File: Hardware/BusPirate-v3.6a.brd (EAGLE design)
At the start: 53.3 x 30.5 mm, 50 parts, among them IC1 PIC24FJ64GA002-I/SSSS-ALTERNA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, IC2 FT232RLSSOP, IC3 4066D, J1 USBSMD

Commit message: First commit of v3.6a
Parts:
- removed C12: 0.1uF, SparkFun:0402-CAP
- removed I/O: M05X2SHD_SMD, SparkFun:2X5-SHROUDED_SMD
- removed J1: USBSMD, SparkFun:USB-MINIB
- removed JP2: LOGO-SFENEW, SparkFun:SFE-NEW-WEBLOGO
- removed JP3, JP4: FIDUCIAL1X2, SparkFun:FIDUCIAL-1X2
- removed LED6: BLUE, SparkFun:LED-0603
- removed LED9: YELLOW, SparkFun:LED-0603
- removed R10, R17: 1k1, SparkFun:0402-RES
- removed R11: 390R, SparkFun:0402-RES
- removed R12, R13, R14, R15, R18, R20, R7, R9: 10k, SparkFun:0402-RES
- removed R16, R8: 2k, SparkFun:0402-RES
- removed VR4: 5V, SparkFun:SOT23-5
- added C3: 0.1uF, SparkFun-Capacitors:0603-CAP
- added FID1, FID2: FIDUCIAL1X2, SparkFun-Aesthetics:FIDUCIAL-1X2
- added FRAME1: FRAME-LETTER, SparkFun-Aesthetics:CREATIVE_COMMONS
- added L1: 700mA+ ferrite, wuerth-elektronik:WE-KI_0805_B
- added LED1A, LED2A, LED3, LED3A, LED4A: (no value), led:CHIP-LED0805
- added LOGO1: SFE_LOGO_NAME_FLAME.1_INCH, SparkFun-Aesthetics:SFE_LOGO_NAME_FLAME_.1
- added LOGO2: OSHW-LOGOL, SparkFun-Aesthetics:OSHW-LOGO-L
- added RN1, RN2, RN3: 10k, Testing:4XARRAY
- added U$3: (no value), dp_devices:DP_LOGO_ART_1X1
- added VR1: MIC5205 3V3, SparkFun-PowerIC:SOT23-5
- C1, C6: value 2.2uF -> 0.1uF; device SparkFun:0402-CAP -> SparkFun-Capacitors:0603-CAP
- C10: value 0.1uF -> 10uF; device SparkFun:0402-CAP -> rcl:SMC_A
- C11: device SparkFun:EIA3216 -> rcl:SMC_A
- C2, C4: device SparkFun:0402-CAP -> SparkFun-Capacitors:0603-CAP
- C5: device SparkFun:0402-CAP -> dp_devices:C603
- C7: value 10uF -> 0.1uF; device SparkFun:EIA3216 -> SparkFun-Capacitors:0603-CAP
- C8: value 2.2uF -> 1uF; device SparkFun:0402-CAP -> dp_devices:C603
- C9: value 0.1uF -> 1uF; device SparkFun:0402-CAP -> dp_devices:C603
- IC1: value PIC24FJ64GA002-I/SSSS-ALTERNATE -> PIC24FJ64GA002; device microchip-pic24:SSOP28DB -> dp_devices:SSOP28
- IC2: value FT232RLSSOP -> FT232RL-BASICSSOP; device SparkFun:SSOP28DB -> SparkFun-DigitalIC:SSOP28DB
- IC3: value 4066D -> 4066; device 40xx:SO14 -> 40xx:TSSOP14
- ICSP: value M05X1PTH -> (none); device SparkFun:1X05 -> SparkFun-Connectors:1X05
- JP1: value LOGO-SFENEW -> (none); device SparkFun:SFE-NEW-WEBLOGO -> SparkFun-Connectors:2X5-SHROUDED_SMD
- LED1, LED4: value RED -> (none); device SparkFun:LED-0603 -> led:CHIP-LED0805
- LED2: value GREEN -> (none); device SparkFun:LED-0603 -> led:CHIP-LED0805
- R1, R5: value 10k -> 2.0k; device SparkFun:0402-RES -> SparkFun-Resistors:0603-RES
- R2: value 1k1 -> 1K; device SparkFun:0402-RES -> SparkFun-Resistors:0603-RES
- R3: value 390R -> 1K; device SparkFun:0402-RES -> SparkFun-Resistors:0603-RES
- R4, R6: value 10k -> 1K; device SparkFun:0402-RES -> SparkFun-Resistors:0603-RES
- U$2: value CREATIVE_COMMONS -> USB-MINIB-5PIN; device SparkFun:CREATIVE_COMMONS -> SparkFun-Connectors:USB-MINIB
- VR2: value 3.3V -> MIC5205 3V3; device SparkFun:SOT23-5 -> SparkFun-PowerIC:SOT23-5
- VR3: value 3.3V -> MIC5205 5V0; device SparkFun:SOT23-5 -> SparkFun-PowerIC:SOT23-5
- moved JP1 53.2 mm to (51.5, 18.5)
- moved C8 31.0 mm to (33.5, 27.0), turned to 270 degrees
- moved U$2 30.1 mm to (5.25, 18.5)
- moved U$1 25.6 mm to (13.3, 2.54), flipped to the top
- moved VR2 22.6 mm to (30.0, 27.0), turned to 270 degrees
- moved C10 20.7 mm to (16.5, 27.0), turned to 270 degrees
- moved C9 19.1 mm to (25.4, 27.0)
- moved R6 18.1 mm to (40.0, 34.5), turned to 180 degrees
- moved LED2 17.8 mm to (35.0, 34.5), turned to 270 degrees
- moved R3 16.9 mm to (20.0, 34.5), turned to 180 degrees
- moved R1 16.7 mm to (21.8, 7.66)
- moved R4 15.8 mm to (30.0, 34.5), turned to 180 degrees
- moved C6 14.8 mm to (17.9, 7.66), turned to 180 degrees
- moved C2 13.1 mm to (25.6, 9.46), turned to 180 degrees
- moved ICSP 12.9 mm to (35.1, 3.50), turned to 180 degrees
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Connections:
- removed net MCLR: IC1.1, ICSP.1, R16.1
- removed net N$10: LED2.C, R17.2
- removed net N$11: IC2.22, R2.1
- removed net N$15: IC2.15, J1.D+
- removed net N$16: IC2.16, J1.D-
- removed net N$8: IC2.23, R17.1
- removed net SWV33: C1.1, I/O.9, R3.1, R4.2, VR3.5
- removed net SWV50: C6.1, I/O.8, R15.2, VR4.5
- removed net TP1: IC1.7
- removed net TP2: IC1.6
- removed net V+: C12.1, C5.1, C7.A, IC2.20, IC3.14, J1.VBUS, LED2.A, LED6.A, R1.2, R10.1, VR2.1, VR2.3, VR3.1, VR4.1
- new net !MCLR: IC1.1, ICSP.5, R1.1
- new net $N26: L1.2, U$2.VBUS
- new net 5V: C10.+, C3.1, C4.1, IC2.20, IC3.14, L1.1, RN3.5, VR1.1, VR1.3, VR2.1, VR3.1
- new net D+: IC2.15, U$2.D+
- new net D-: IC2.16, U$2.D-
- new net RXLED: IC2.22, LED4.C, LED4A.C
- new net SW3V3: C8.1, JP1.2, R6.2, RN1.6, VR2.5
- new net SW5V0: C9.1, JP1.3, RN1.8, VR3.5
- net ADC: now also JP1.4, RN2.6; no longer I/O.7, R7.2
- net ADC1: now also RN2.3, RN2.4; no longer R6.1, R7.1
- net ADC2: now also RN2.1, RN2.2; no longer R12.1, R13.1
- net ADC3: now also RN1.3, RN1.4; no longer R4.1, R5.1
- net ADC4: now also RN1.1, RN1.2; no longer R14.1, R15.1
- net AUX1: now also JP1.6; no longer I/O.5
- net CLK: now also JP1.7, RN3.1; no longer I/O.4, R9.2
- net CS: now also JP1.9, RN3.3; no longer I/O.2, R18.2
- net GND: now also C10.-, C11.-, C3.2, C7.2, IC1.6, IC1.7, JP1.1, LED1A.C, LED2.C, LED2A.C, LED3.C, LED3A.C, RN1.5, RN1.7, RN2.5, RN2.7, U$2.GND, VR1.2; no longer C10.2, C11.C, C12.2, C7.C, I/O.10, J1.GND, LED4.C, LED9.C, R13.2, R14.2, R5.2, R6.2, VR4.2
- net LD1: now also R4.2; no longer R11.1
- net MISO: now also JP1.10, RN3.2; no longer I/O.1, R20.2
- net MOSI: now also JP1.8, R5.1; no longer I/O.3, R8.2
- net N$1: now also R5.2; no longer R8.1
- net N$13: now also LED4.A, LED4A.A, R3.1; no longer LED6.C, R2.2
- net N$18: now also LED3.A, LED3A.A, R6.1; no longer LED9.A, R3.2
- net N$2: now also IC3.9, RN3.6; no longer IC3.3, R9.1
- net N$3: now also C11.+; no longer C11.A
- net N$4: now also RN3.7; no longer R20.1
- net N$5: now also IC3.3, RN3.8; no longer IC3.9, R18.1
- net N$6: now also LED2.A, LED2A.A, R4.1; no longer LED4.A, R11.2
- net N$7: now also LED1A.A, R2.1; no longer R10.2
- net N$9: now also C5.1; no longer C9.1
- net PGC: now also ICSP.1; no longer ICSP.5
- net PGD: now also ICSP.2; no longer ICSP.4
- net PULLUPEN: now also RN3.4; no longer R1.1
- net VCC: now also C1.1, C6.1, C7.1, ICSP.4, R1.2, R2.2, R3.2, VR1.5; no longer C10.1, C4.1, C8.1, ICSP.2, R16.2, VR2.5
- net VEXTERN: now also JP1.5, RN2.8; no longer I/O.6, R12.2
- net VREGEN: now also VR2.3; no longer VR4.3
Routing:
- net V+: track 111.2 -> 0.00 mm, vias 5 -> 0
- net 5V: track 0.00 -> 66.5 mm, vias 0 -> 4
- net SW3V3: track 0.00 -> 45.7 mm
- net SWV50: track 42.2 -> 0.00 mm, vias 3 -> 0
- net SW5V0: track 0.00 -> 40.2 mm, vias 0 -> 3
- net RXLED: track 0.00 -> 32.7 mm, vias 0 -> 2
- net SWV33: track 32.2 -> 0.00 mm
- net VCC: track 89.8 -> 115.1 mm, vias 4 -> 3
- net !MCLR: track 0.00 -> 22.1 mm, vias 0 -> 2
- net N$8: track 22.0 -> 0.00 mm, vias 2 -> 0
- net N$11: track 21.5 -> 0.00 mm, vias 2 -> 0
- net MCLR: track 19.8 -> 0.00 mm, vias 2 -> 0
- net D-: track 0.00 -> 9.90 mm
- net N$5: track 7.16 -> 17.1 mm, vias 0 -> 2
- net N$1: track 12.5 -> 22.1 mm, vias 0 -> 2
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- added copper zone on layer 1, net $N26
- added copper zone on layer 1, net 5V
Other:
- board size 53.3 x 30.5 mm -> 60 x 37 mm
- board text added: "!MLCR"
- board text added: "+3V3"
- board text added: "2011"
- board text added: "3V3"
- board text added: "All units in mm"
- board text added: "BPv3.6a"
- board text added: "I+S"
- board text added: "Ian Lesnet http://dangerousprototypes.com"
- board text added: "JUN 2012"
- board text added: "Revised by: Brent Wilkins (Based on BP v3.6a)"
- board text added: "VPU"
- board text added: "v.trocio"
- board text added: "v01"
- board text added: "v3.6a"
- board text removed: "+3.3V"
- board text removed: "+3v"
- board text removed: "+5v"
- board text removed: "2/10/2010"
- board text removed: "AUX1"
- board text removed: "BPv3"
- board text removed: "BPv3a"
- board text removed: "Based on design by"
- board text removed: "CLOCK"
- board text removed: "DATA"
- board text removed: "DangerousPrototypes.com"
- board text removed: "Fulfillment by"
- board text removed: "ICSP"
- board text removed: "Layout for SparkFun Electronics by Chris Taylor"
- board text removed: "RX"
- board text removed: "SEP 2009"
- board text removed: "Seeed Studio"
- board text removed: "TX"
- board text removed: "VCC"
- board text removed: "Vpu"
- board text removed: "dangerousprototypes.com"
- board text removed: "www.seeedstudio.com"

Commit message: Finished inital DFM
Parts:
- removed IC3: 4066, 40xx:TSSOP14
- removed LED1A, LED2A, LED3A, LED4A: (no value), led:CHIP-LED0805
- removed RN1, RN2: 10k, Testing:4XARRAY
- added LED5, LED6, LED7, LED8: RED, SparkFun-LED:LED-0603
- added R10, R11: 2.0k, SparkFun-Resistors:0603-RES
- added R7, R9: 1K, SparkFun-Resistors:0603-RES
- added R8: 0.27, SparkFun-Resistors:0603
- added U3: PIC24FJ64GA002, Testing:SSOP28
- C10, C11: value 10uF -> 0.1uF; device rcl:SMC_A -> SparkFun-Capacitors:0603-CAP
- C3, C4, C7: value 0.1uF -> 10uF; device SparkFun-Capacitors:0603-CAP -> SparkFun-Capacitors:0805-CAP
- C5: device dp_devices:C603 -> SparkFun-Capacitors:0603-CAP
- C8, C9: value 1uF -> 10uF; device dp_devices:C603 -> SparkFun-Capacitors:0805-CAP
- IC1: value PIC24FJ64GA002 -> 4066; device dp_devices:SSOP28 -> 40xx:TSSOP14
- L1: value 700mA+ ferrite -> 1A Ferrite; device wuerth-elektronik:WE-KI_0805_B -> SparkFun-Passives:0603
- LED1, LED2, LED3, LED4: value (none) -> RED; device led:CHIP-LED0805 -> SparkFun-LED:LED-0603
- LOGO1: value SFE_LOGO_NAME_FLAME.1_INCH -> OSHW-LOGOL; device SparkFun-Aesthetics:SFE_LOGO_NAME_FLAME_.1 -> SparkFun-Aesthetics:OSHW-LOGO-L
- LOGO2: value OSHW-LOGOL -> SFE_LOGO_NAME_FLAME.1_INCH; device SparkFun-Aesthetics:OSHW-LOGO-L -> SparkFun-Aesthetics:SFE_LOGO_NAME_FLAME_.1
- R1, R5: value 2.0k -> 0.27; device SparkFun-Resistors:0603-RES -> SparkFun-Resistors:0603
- R2, R3: value 1K -> 10k; device SparkFun-Resistors:0603-RES -> Testing:4XARRAY
- moved C3 48.2 mm to (4.47, 26.9), turned to 270 degrees
- moved R2 32.2 mm to (41.1, 26.1), turned to 270 degrees
- moved C6 30.8 mm to (48.6, 7.55), turned to 0 degrees
- moved LED3 30.0 mm to (15.0, 34.5)
- moved R6 30.0 mm to (10.0, 34.5)
- moved C7 29.1 mm to (32.9, 27.0)
- moved R1 27.0 mm to (2.95, 26.9), turned to 270 degrees
- moved C11 25.3 mm to (11.9, 16.6), turned to 270 degrees
- moved R3 25.1 mm to (41.1, 21.0), turned to 270 degrees
- moved C4 19.8 mm to (16.5, 27.3), turned to 270 degrees
- moved C10 19.4 mm to (17.9, 7.66), turned to 180 degrees
- moved IC1 16.9 mm to (43.7, 5.63)
- moved C9 16.2 mm to (36.7, 15.3), turned to 45 degrees
- moved R5 14.0 mm to (34.5, 27.0), turned to 270 degrees
- moved LOGO1 13.4 mm to (9.78, 18.5), flipped to the bottom
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- renumbered IC2 to U5, ICSP to JP2, RN3 to R12, U$2 to J1, VR1 to U1, VR2 to U2, VR3 to U4
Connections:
- new net N$10: C7.2, R5.2
- new net N$11: C8.2, R8.2
- new net N$8: C3.2, R1.2
- net !MCLR: now also R10.1, U3.1; no longer IC1.1, R1.1
- net $N26: now also L1.1; no longer L1.2
- net 5V: now also C5.1, C6.1, IC1.14, L1.2; no longer C10.+, C3.1, IC3.14, L1.1
- net ADC: now also R3.6; no longer RN2.6
- net ADC1: now also R3.3, R3.4, U3.23; no longer IC1.23, RN2.3, RN2.4
- net ADC2: now also R3.1, R3.2, U3.24; no longer IC1.24, RN2.1, RN2.2
- net ADC3: now also R2.3, R2.4, U3.25; no longer IC1.25, RN1.3, RN1.4
- net ADC4: now also R2.1, R2.2, U3.26; no longer IC1.26, RN1.1, RN1.2
- net AUX1: now also U3.21; no longer IC1.21
- net CLK: now also U3.17; no longer IC1.17
- net CS: now also U3.15; no longer IC1.15
- net CTS: now also U3.10; no longer IC1.10
- net GND: now also C10.2, C11.2, LED4.C, LED5.C, LED6.C, LED7.C, LED8.C, R1.1, R2.5, R2.7, R3.5, R3.7, R5.1, R8.1, U3.19, U3.27, U3.6, U3.7, U3.8; no longer C10.-, C11.-, C3.2, C7.2, C8.2, IC1.19, IC1.27, IC1.6, IC1.8, IC3.7, LED1.C, LED1A.C, LED2.C, LED2A.C, LED3A.C, RN1.5, RN1.7, RN2.5, RN2.7
- net LD1: now also R7.2, U3.3; no longer IC1.3, R4.2
- net MISO: now also U3.16; no longer IC1.16
- net MOSI: now also R11.1, U3.18; no longer IC1.18, R5.1
- net N$1: now also IC1.2, R11.2; no longer IC3.2, R5.2
- net N$13: now also LED1.A, LED2.A, R4.1; no longer LED4.A, LED4A.A, R3.1
- net N$18: now also LED7.A, LED8.A, R9.1; no longer LED3.A, LED3A.A, R6.1
- net N$2: now also IC1.9; no longer IC3.9
- net N$3: now also C9.1, U3.20; no longer C11.+, IC1.20
- net N$4: now also IC1.10; no longer IC3.10
- net N$5: now also IC1.3; no longer IC3.3
- net N$6: now also LED5.A, LED6.A, R7.1; no longer LED2.A, LED2A.A, R4.1
- net N$7: now also LED3.A, LED4.A, R6.1; no longer LED1.A, LED1A.A, R2.1
- net N$9: now also C11.1; no longer C5.1
- net PGC: now also U3.5; no longer IC1.5
- net PGD: now also U3.4; no longer IC1.4
- net PULLUPEN: now also IC1.12, IC1.13, IC1.5, IC1.6, U3.22; no longer IC1.22, IC3.12, IC3.13, IC3.5, IC3.6
- net RTS: now also U3.12; no longer IC1.12
- net RX: now also U3.11; no longer IC1.11
- net RXLED: now also LED1.C, LED2.C; no longer LED4.C, LED4A.C
- net SW3V3: now also C7.1, R2.6, R9.2; no longer C8.1, R6.2, RN1.6
- net SW5V0: now also C8.1, R2.8; no longer C9.1, RN1.8
- net TP0: now also U3.9; no longer IC1.9
- net TX: now also U3.14; no longer IC1.14
- net VCC: now also C10.1, C3.1, R10.2, R4.2, R6.2, U3.13, U3.28; no longer C6.1, C7.1, IC1.13, IC1.28, R1.2, R2.2, R3.2
- net VEXTERN: now also IC1.1, IC1.11, IC1.4, IC1.8, R3.8; no longer IC3.1, IC3.11, IC3.4, IC3.8, RN2.8
- net VREGEN: now also U3.2; no longer IC1.2
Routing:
- net N$10: track 0.00 -> 1.72 mm
- net N$11: track 0.00 -> 1.67 mm
- net N$8: track 0.00 -> 1.56 mm
- net SW3V3: track 45.7 -> 45.2 mm
- net MISO: track 28.0 -> 28.5 mm
- net VCC: track 115.1 -> 114.6 mm
- net GND: vias 54 -> 56

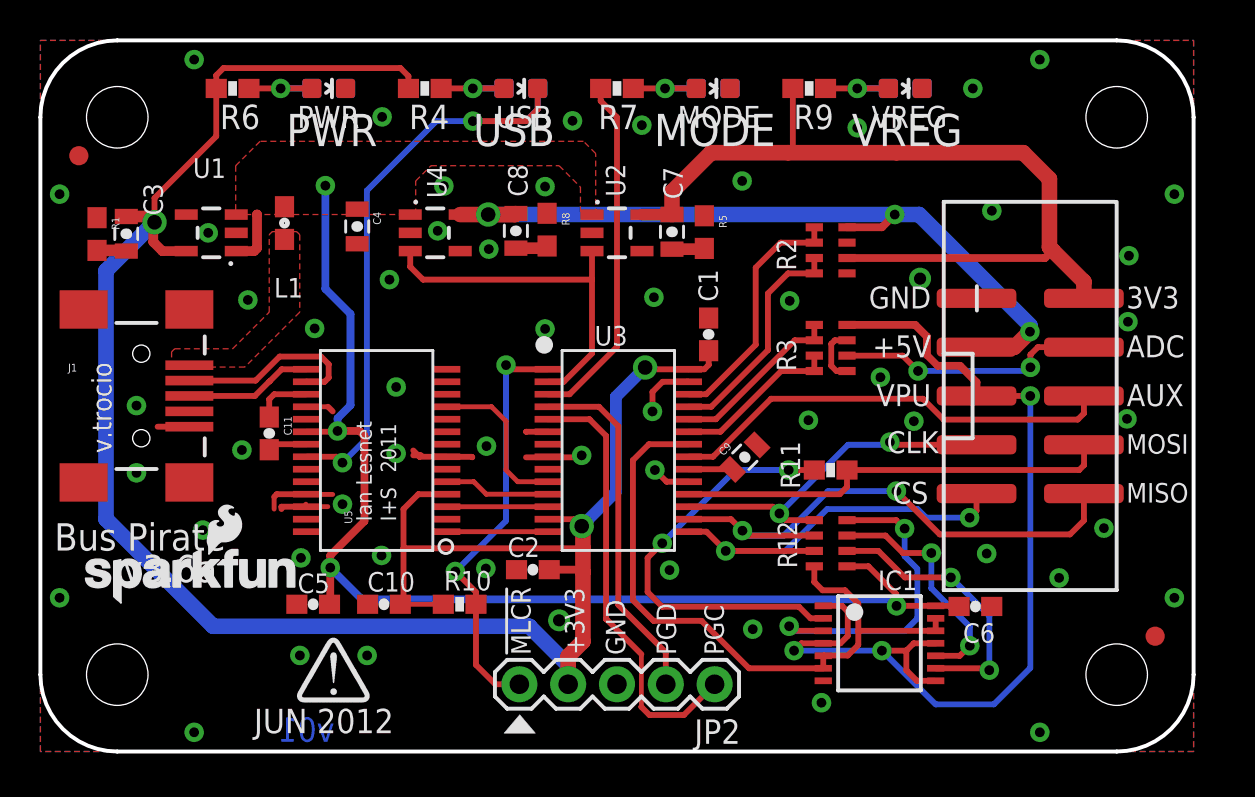
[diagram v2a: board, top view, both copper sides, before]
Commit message: Changed from SFE to DP versioning, and changed bottom LEDs to DNP
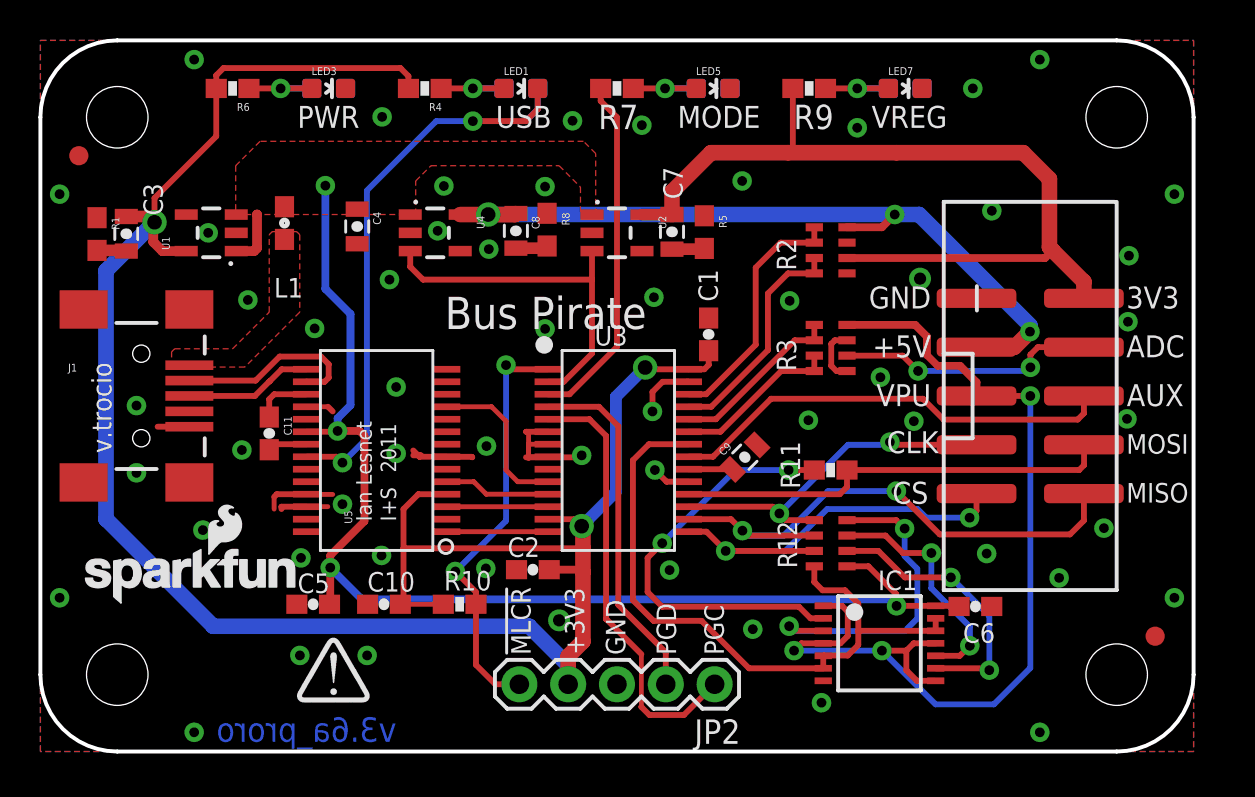
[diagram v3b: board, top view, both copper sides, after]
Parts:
- LED2, LED4, LED6, LED8: value RED -> DNP
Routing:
- net GND: track 27.9 -> 32.8 mm
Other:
- board text added: "v3.6a_proro"
- board text removed: "JUN 2012"
- board text removed: "v01"
- board text removed: "v3.6a"

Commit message: Changed license from CC4 to CC0
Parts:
- removed FRAME1: FRAME-LETTER, SparkFun-Aesthetics:CREATIVE_COMMONS
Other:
- board text added: "Designed by: Ian Lesnet http://dangerousprototypes.com"
- board text added: "Released under the Creative Commons 0 "No Rights Reserved""
- board text added: "https://creativecommons.org/publicdomain/zero/1.0/"
- board text removed: "Ian Lesnet http://dangerousprototypes.com"
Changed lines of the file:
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@@
 <layers>
 <layer number="1" name="Top" color="4" fill="1" visible="yes" active="yes"/>
+<layer number="2" name="Route2" color="1" fill="3" visible="yes" active="yes"/>
+<layer number="3" name="Route3" color="4" fill="3" visible="yes" active="yes"/>
+<layer number="4" name="Route4" color="1" fill="4" visible="yes" active="yes"/>
+<layer number="5" name="Route5" color="4" fill="4" visible="yes" active="yes"/>
+<layer number="6" name="Route6" color="1" fill="8" visible="yes" active="yes"/>
+<layer number="7" name="Route7" color="4" fill="8" visible="yes" active="yes"/>
+<layer number="8" name="Route8" color="1" fill="2" visible="yes" active="yes"/>
+<layer number="9" name="Route9" color="4" fill="2" visible="yes" active="yes"/>
+<layer number="10" name="Route10" color="1" fill="7" visible="yes" active="yes"/>
+<layer number="11" name="Route11" color="4" fill="7" visible="yes" active="yes"/>
+<layer number="12" name="Route12" color="1" fill="5" visible="yes" active="yes"/>
+<layer number="13" name="Route13" color="4" fill="5" visible="yes" active="yes"/>
+<layer number="14" name="Route14" color="1" fill="6" visible="yes" active="yes"/>
+<layer number="15" name="Route15" color="4" fill="6" visible="yes" active="yes"/>
 <layer number="16" name="Bottom" color="1" fill="1" visible="yes" active="yes"/>
 <layer number="17" name="Pads" color="2" fill="1" visible="yes" active="yes"/>
@@
 <dimension x1="4" y1="4" x2="4" y2="0" x3="-4" y3="2" textsize="1.778" textratio="15" layer="47"/>
 <text x="30" y="43" size="1.778" layer="47" font="vector" ratio="10" align="bottom-center">All units in mm</text>
-<text x="22.86" y="-19.05" size="1.778" layer="51">Ian Lesnet http://dangerousprototypes.com</text>
-<text x="3.77825" y="-21.62175" size="1.778" layer="51">Revised by: Brent Wilkins (Based on BP v3.6a)</text>
+<text x="29.845" y="-13.97" size="1.778" layer="51" font="vector" align="bottom-center">Designed by: Ian Lesnet http://dangerousprototypes.com</text>
+<text x="29.845" y="-16.54175" size="1.778" layer="51" font="vector" align="bottom-center">Revised by: Brent Wilkins (Based on BP v3.6a)</text>
 <text x="13.843" y="0.508" size="1.27" layer="16" font="vector" ratio="18" rot="MR0" align="bottom-center">v3.6a_proro</text>
 <text x="14.986" y="33.02" size="1.143" layer="21" font="vector" ratio="15" align="center">PWR</text>
@@
 <rectangle x1="26.1493" y1="16.2179" x2="26.7081" y2="16.4465" layer="41"/>
 <rectangle x1="13.589" y1="12.9286" x2="14.0716" y2="13.1572" layer="41"/>
+<text x="29.845" y="-8.89" size="1.778" layer="51" font="vector" align="bottom-center">Released under the Creative Commons 0 "No Rights Reserved"</text>
+<text x="29.845" y="-11.43" size="1.778" layer="51" font="vector" align="bottom-center">https://creativecommons.org/publicdomain/zero/1.0/</text>
 </plain>
 <attributes>
@@
 </element>
 <element name="U$3" library="dp_devices" package="DP_LOGO_ART_1X1" value="" x="42.487" y="8.2385" rot="MR0"/>
-<element name="FRAME1" library="SparkFun-Aesthetics" package="CREATIVE_COMMONS" value="FRAME-LETTER" x="-7.62" y="-19.05"/>
 <element name="LOGO2" library="SparkFun-Aesthetics" package="SFE_LOGO_NAME_FLAME_.1" value="SFE_LOGO_NAME_FLAME.1_INCH" x="1.905" y="7.62"/>
 <element name="LOGO1" library="SparkFun-Aesthetics" package="OSHW-LOGO-L" value="OSHW-LOGOL" x="9.779" y="18.5" rot="MR0"/>
